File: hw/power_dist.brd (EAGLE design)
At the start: 80 x 50 mm, 72 parts, among them J1 JST-ZH6SMT_VERT, J2 JST-PH4SMT_VERT, J3 JST-PH5VERT, P1 XT30P, P2 XT30P, P3 XT30P, P4 XT30P, P5 XT30P, P6 XT30P, P7 XT90PW-M, Q1 PSMN4R8-100BSEJ, Q2 PSMN4R8-100BSEJ, Q3 PSMN4R8-100BSEJ, Q4 MF-DSC-SOT233-BSS138, Q5 MF-DSC-SOT233-MMBT3906, Q6 MF-DSC-SOT233-MMBT3904, U1 MAX15062AATA+T, U2 STM32G474CEU6, U3 LM5066IPMHE/NOPB, U4 TCAN334G

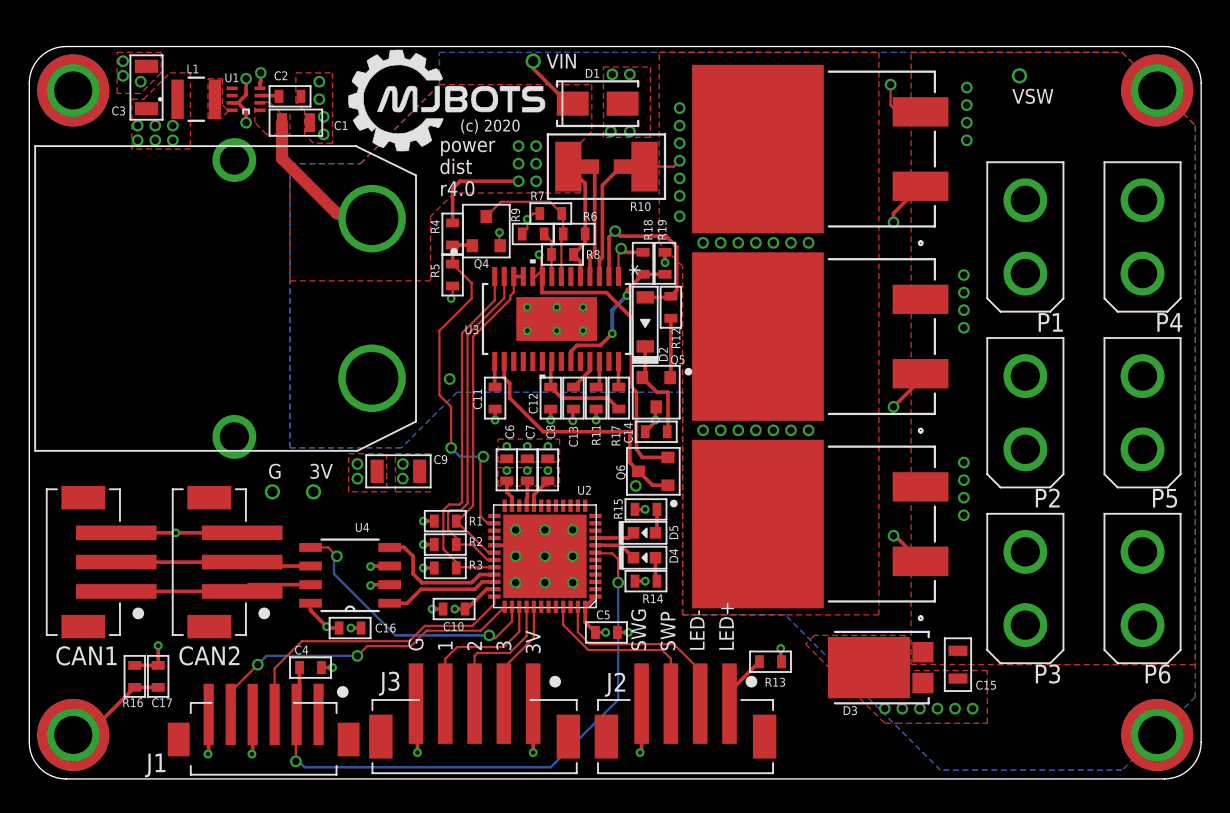
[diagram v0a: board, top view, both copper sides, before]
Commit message: Work towards functioning r4
* Beginnings of firmware
* Initial README and CHANGES
* Start on r4.1 w/ fixed D3 footprint
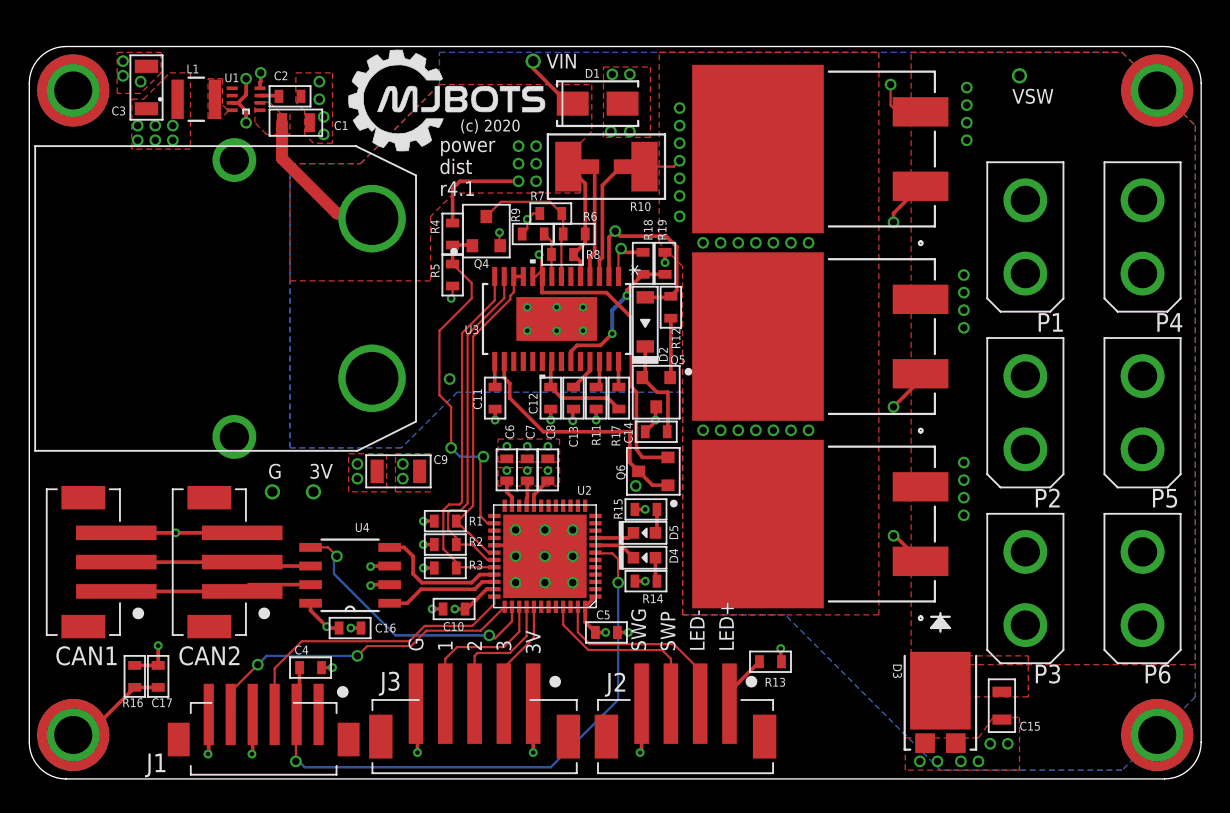
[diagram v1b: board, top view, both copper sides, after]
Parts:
- D3: value FSV10150V -> FSV10150VTO277-3L_ONS-L; device power_dist:TO277-3L_ONS -> power_dist:TO277-3L_ONS-L
- moved D3 4.66 mm to (62.2, 5.20), turned to 0 degrees
- moved C15 4.10 mm to (66.4, 5.00)
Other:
- board text added: "power dist r4.1"
- board text removed: "power dist r4.0"
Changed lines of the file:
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@@
 <text x="28" y="43.8" size="1" layer="21" font="vector" align="top-left">power
 dist
-r4.0</text>
+r4.1</text>
 <text x="29.4" y="45" size="0.8" layer="21" font="vector" ratio="10" align="top-left">(c) 2020</text>
 <polygon width="0.05" layer="25">
@@
 <attribute name="VENDOR" value="Vishay" x="38.8" y="46.1" size="1.778" layer="27" display="off"/>
 </element>
-<element name="D3" library="power_dist" package="TO277-3L_ONS" value="FSV10150V" x="58.2" y="7.6" smashed="yes" rot="R90">
-<attribute name="BUILT_BY" value="EMA_Jessica" x="58.2" y="7.6" size="1.778" layer="27" rot="R90" display="off"/>
-<attribute name="COPYRIGHT" value="Copyright (C) 2018 Accelerated Designs. All rights reserved" x="58.2" y="7.6" size="1.778" layer="27" rot="R90" display="off"/>
-<attribute name="MANUFACTURER_PART_NUMBER" value="FSV10150V" x="58.2" y="7.6" size="1.778" layer="27" rot="R90" display="off"/>
-<attribute name="MPN" value="FSV10150V" x="58.2" y="7.6" size="1.778" layer="27" rot="R90" display="off"/>
-<attribute name="NAME" x="55.5234" y="4.365" size="0.6" layer="25" ratio="10" rot="SR0"/>
-<attribute name="POPULATE" value="1" x="58.2" y="7.6" size="1.778" layer="27" rot="R90" display="off"/>
-<attribute name="SOURCELIBRARY" value="ON_Semiconductor_2019-12-30" x="58.2" y="7.6" size="1.778" layer="27" rot="R90" display="off"/>
-<attribute name="VENDOR" value="ON Semiconductor" x="58.2" y="7.6" size="1.778" layer="27" rot="R90" display="off"/>
+<element name="D3" library="power_dist" package="TO277-3L_ONS-L" value="FSV10150VTO277-3L_ONS-L" x="62.2" y="5.2" smashed="yes">
+<attribute name="BUILT_BY" value="EMA_Jessica" x="62.2" y="5.2" size="1.778" layer="27" display="off"/>
+<attribute name="COPYRIGHT" value="Copyright (C) 2018 Accelerated Designs. All rights reserved" x="62.2" y="5.2" size="1.778" layer="27" display="off"/>
+<attribute name="MANUFACTURER_PART_NUMBER" value="FSV10150V" x="62.2" y="5.2" size="1.778" layer="27" display="off"/>
+<attribute name="MPN" value="FSV10150V" x="62.2" y="5.2" size="1.778" layer="27" display="off"/>
+<attribute name="NAME" x="58.965" y="7.8766" size="0.6" layer="25" ratio="10" rot="SR270"/>
+<attribute name="POPULATE" value="1" x="62.2" y="5.2" size="1.778" layer="27" display="off"/>
+<attribute name="SOURCELIBRARY" value="ON_Semiconductor_2019-12-30" x="62.2" y="5.2" size="1.778" layer="27" display="off"/>
+<attribute name="VENDOR" value="ON Semiconductor" x="62.2" y="5.2" size="1.778" layer="27" display="off"/>
 </element>
 <element name="Q1" library="power_dist" package="D2PAK_SOT404_NEX" value="PSMN4R8-100BSEJ" x="54" y="30.2" smashed="yes" rot="R90">
@@
 <attribute name="POPULATE" value="1" x="39.4" y="41.8" size="1.778" layer="27" display="off"/>
 </element>
-<element name="C15" library="mfpassives" package="C0805" value="1uF 100V" x="63.4" y="7.8" smashed="yes" rot="R270">
-<attribute name="DIELECTRIC" value="" x="63.4" y="7.8" size="1.778" layer="27" rot="R270" display="off"/>
-<attribute name="HOUSEPART" value="" x="63.4" y="7.8" size="1.778" layer="27" rot="R270" display="off"/>
-<attribute name="MF" value="MURATA" x="63.4" y="7.8" size="1.778" layer="27" rot="R270" display="off"/>
-<attribute name="MPN" value="GCM21BC72A105KE36L" x="63.4" y="7.8" size="1.778" layer="27" rot="R270" display="off"/>
-<attribute name="NAME" x="64.6" y="6.1" size="0.6" layer="25" font="vector" ratio="10"/>
-<attribute name="POPULATE" value="1" x="63.4" y="7.8" size="1.778" layer="27" rot="R270" display="off"/>
-<attribute name="TOLERANCE" value="" x="63.4" y="7.8" size="1.778" layer="27" rot="R270" display="off"/>
-<attribute name="URL" value="" x="63.4" y="7.8" size="1.778" layer="27" rot="R270" display="off"/>
-<attribute name="VOLTAGE" value="" x="63.4" y="7.8" size="1.778" layer="27" rot="R270" display="off"/>
+<element name="C15" library="mfpassives" package="C0805" value="1uF 100V" x="66.4" y="5" smashed="yes" rot="R270">
+<attribute name="DIELECTRIC" value="" x="66.4" y="5" size="1.778" layer="27" rot="R270" display="off"/>
+<attribute name="HOUSEPART" value="" x="66.4" y="5" size="1.778" layer="27" rot="R270" display="off"/>
+<attribute name="MF" value="MURATA" x="66.4" y="5" size="1.778" layer="27" rot="R270" display="off"/>
+<attribute name="MPN" value="GCM21BC72A105KE36L" x="66.4" y="5" size="1.778" layer="27" rot="R270" display="off"/>
+<attribute name="NAME" x="67.6" y="3.3" size="0.6" layer="25" font="vector" ratio="10"/>
+<attribute name="POPULATE" value="1" x="66.4" y="5" size="1.778" layer="27" rot="R270" display="off"/>
+<attribute name="TOLERANCE" value="" x="66.4" y="5" size="1.778" layer="27" rot="R270" display="off"/>
+<attribute name="URL" value="" x="66.4" y="5" size="1.778" layer="27" rot="R270" display="off"/>
+<attribute name="VOLTAGE" value="" x="66.4" y="5" size="1.778" layer="27" rot="R270" display="off"/>
 </element>
 <element name="J3" library="power_dist" package="JST_B5B_PH-SM4-TB(LF)(SN)" value="JST-PH5VERT" x="30.4" y="2.6" smashed="yes" rot="R180">
@@
 <contactref element="C3" pad="P$2"/>
 <contactref element="D1" pad="2"/>
+<contactref element="D3" pad="1"/>
 <contactref element="D3" pad="2"/>
-<contactref element="D3" pad="1"/>
 <contactref element="R9" pad="P$2"/>
 <contactref element="R7" pad="P$2"/>
@@
 <vertex x="39.2" y="43.8"/>
 </polygon>
-<via x="58.4" y="4.8" extent="1-16" drill="0.5"/>
-<via x="59.6" y="4.8" extent="1-16" drill="0.5"/>
-<via x="60.8" y="4.8" extent="1-16" drill="0.5"/>
-<via x="62" y="4.8" extent="1-16" drill="0.5"/>
-<via x="63.2" y="4.8" extent="1-16" drill="0.5"/>
-<via x="64.4" y="4.8" extent="1-16" drill="0.5"/>
-<polygon width="0.1524" layer="1" thermals="no">
-<vertex x="53" y="9.2"/>
-<vertex x="58.4" y="3.8"/>
-<vertex x="59.2" y="3.8"/>
-<vertex x="65.4" y="3.8"/>
-<vertex x="65.4" y="7.4"/>
-<vertex x="59.8" y="7.4"/>
-<vertex x="59.8" y="9.8"/>
-<vertex x="53.6" y="9.8"/>
-</polygon>
+<via x="60.8" y="1.2" extent="1-16" drill="0.5"/>
+<via x="62" y="1.2" extent="1-16" drill="0.5"/>
+<via x="63.6" y="1.2" extent="1-16" drill="0.5"/>
+<via x="64.8" y="1.2" extent="1-16" drill="0.5"/>
+<via x="65.6" y="2.4" extent="1-16" drill="0.5"/>
+<via x="66.8" y="2.4" extent="1-16" drill="0.5"/>
 <contactref element="Q6" pad="P$2"/>
 <via x="34" y="32.2" extent="1-16" drill="0.3048"/>
@@
 <via x="43.4" y="35.25" extent="1-16" drill="0.3048"/>
 <wire x1="43.4" y1="35.95" x2="43.4" y2="35.25" width="0.254" layer="1"/>
+<polygon width="0.1524" layer="1" thermals="no">
+<vertex x="59.8" y="2.8"/>
+<vertex x="64.8" y="2.8"/>
+<vertex x="65.8" y="4.2"/>
+<vertex x="67.6" y="4.2"/>
+<vertex x="67.6" y="0.6"/>
+<vertex x="59.8" y="0.6"/>
+</polygon>
 </signal>
 <signal name="VCC" class="1">
@@
 <wire x1="41.9" y1="35.95" x2="40.65" y2="35.95" width="0.254" layer="1"/>
 <wire x1="40.65" y1="35.95" x2="40.4" y2="36.2" width="0.254" layer="1"/>
+<polygon width="0.1524" layer="1" thermals="no">
+<vertex x="61.4" y="8.4"/>
+<vertex x="68.2" y="8.4"/>
+<vertex x="68.2" y="5.6"/>
+<vertex x="61.4" y="5.6"/>
+</polygon>
 </signal>
 <signal name="VIN_SENSE">

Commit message: Draft r4.1 based on the LTC4380
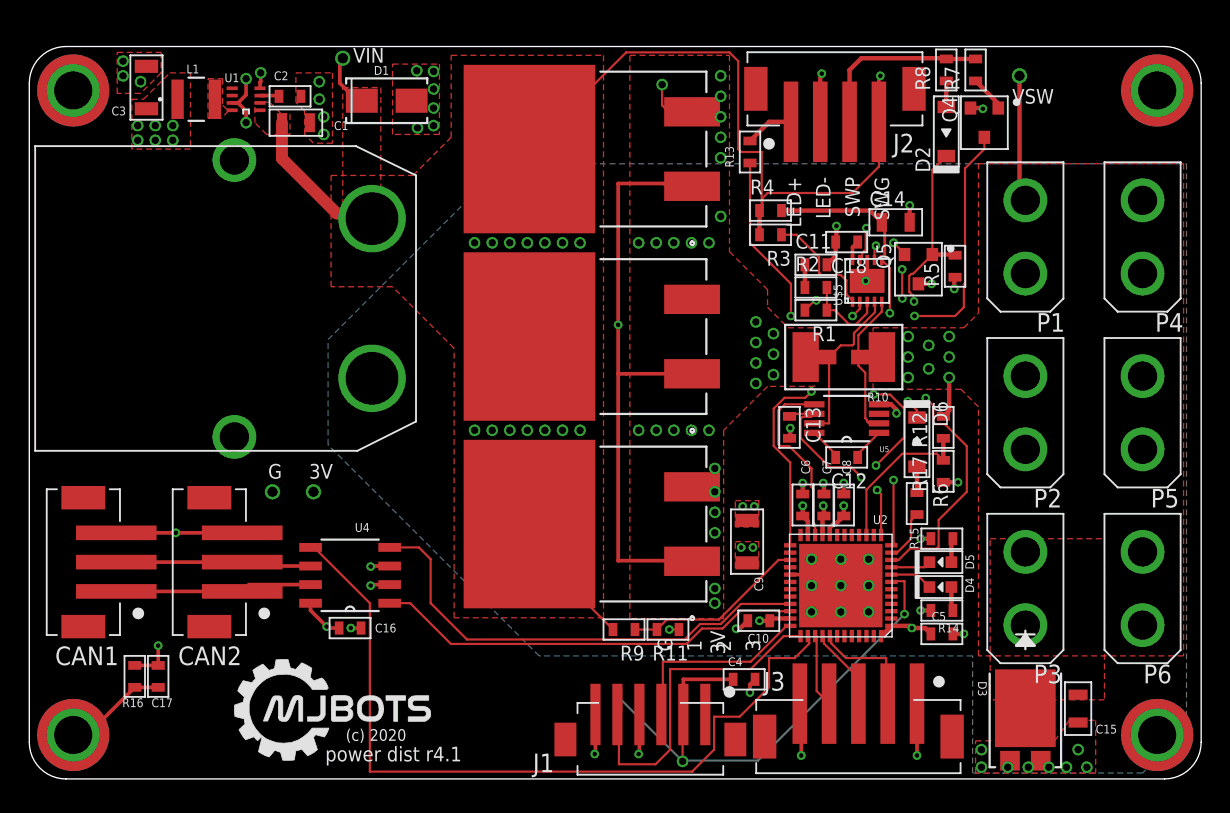
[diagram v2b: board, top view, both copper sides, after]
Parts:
- removed Q6: MF-DSC-SOT233-MMBT3904, mfdiscretesemi:SOT-23-3
- removed R18, R19: DNP, mfpassives:R0603
- removed U3: LM5066IPMHE/NOPB, power_dist:MXA28A_TEX
- added C18: 0.1uF, mfpassives:C0603
- added D6: MF-DIO-SOD123-1N4148, mfdiscretesemi:SOD-123
- added U$5: LTC4830, power_dist:DFN10
- added U5: LT1787HVIMS8PBF, LT1787HVIMS8PBF:MSOP-8_MS
- C11: value 1uF -> (none)
- C12: value 1uF -> DNP
- C13: value 0.01uF -> 0.1uF
- C14: value 0.01uF -> 1uF 100V; device mfpassives:C0603 -> mfpassives:C0805
- Q4: value MF-DSC-SOT233-BSS138 -> MF-DSC-SOT233-MMBT3904
- Q5: value MF-DSC-SOT233-MMBT3906 -> MMBT5401 100V
- R1, R2, R3: value 10k -> (none)
- R10: value 0.3mOhm -> 0.5mOhm
- R11: value 24k 1% -> 200k 1%
- R12: value 1k 1% -> 3M 1%
- R17: value DNP -> 200k 1%
- R4: value 140k 1% -> 10k
- R5: value 40.2k 1% -> 200k
- R6: value 100k 1% -> 1k
- R7: value 40.2k 1% -> 2M
- R8: value 140k 1% -> 500k
- R9: value 6.49k 1% -> 3M 1%
- moved J2 45.9 mm to (55.0, 47.4), turned to 0 degrees
- moved R13 34.8 mm to (49.2, 42.8), turned to 270 degrees
- moved Q4 34.8 mm to (65.2, 44.8), turned to 270 degrees
- moved R5 34.3 mm to (63.2, 35.0), turned to 90 degrees
- moved R3 31.8 mm to (50.6, 37.1)
- moved R2 30.8 mm to (53.7, 33.5), turned to 0 degrees
- moved R7 30.6 mm to (64.6, 48.4), turned to 90 degrees
- moved R6 29.8 mm to (60.6, 18.8), turned to 270 degrees
- moved C4 29.6 mm to (48.8, 6.80)
- moved R1 29.1 mm to (53.7, 32.0)
- moved R8 29.1 mm to (62.6, 48.4), turned to 90 degrees
- moved R9 27.7 mm to (40.6, 10.2)
- moved J1 26.4 mm to (42.4, 2.40)
- moved J3 26.2 mm to (56.6, 2.60)
- moved D2 24.3 mm to (62.6, 44.2)
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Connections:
- removed net N$16: Q5.P$1, R12.P$2
- removed net N$3: Q6.P$1, Q6.P$3, U3.16
- removed net PSHDN: Q4.P$1, R4.P$2, R5.P$1, U2.26
- removed net SCL: R2.P$1, U2.31, U3.13
- removed net SDA: R1.P$1, U2.30, U3.11, U3.12
- removed net SMBA: R3.P$1, U2.32, U3.14
- removed net VDD: C12.P$1, R17.P$1, U3.21
- removed net VIN_SENSE: R8.P$2, R9.P$1, U3.8
- new net FLT: U$5.7, U2.13
- new net GATE: Q1.1, Q2.1, Q3.1, R1.P$2
- new net ISAMP: U2.22, U5.5
- new net ISAMP_BIAS: C13.P$1, U2.12, U5.6
- new net LTC_EN: Q5.P$2, U$5.9
- new net LTC_VCC: C14.P$1, R4.P$2, U$5.2, U$5.6
- new net N$17: D2.ANODE, R8.P$1
- new net N$18: D6.ANODE, R6.P$1
- new net PGND: C15.P$2, D3.1, D3.2, P1.1, P2.1, P3.1, P4.1, P5.1, P6.1, P7.1
- new net PWR_OVERRIDE: R6.P$2, U2.11
- new net SNS_PWR_SW: Q4.P$3, U2.10
- new net VIN_SAMP: R11.P$2, R9.P$1, U2.27
- new net VSWITCHED_SAMP: R12.P$1, R17.P$2, U2.15
- net +24V: now also J2.4, Q1.2, Q2.2, Q3.2, R3.P$2, R9.P$2; no longer R10.1, R6.P$1, R8.P$1, U3.5
- net GND: now also C18.P$2, J2.2, R11.P$1, R17.P$1, R5.P$1, U$5.8, U$5.P$1, U5.4; no longer C12.P$2, C15.P$2, D3.1, D3.2, J2.4, P1.1, P2.1, P3.1, P4.1, P5.1, P6.1, P7.1, Q6.P$2, R11.P$2, R19.P$2, R5.P$2, R7.P$2, R9.P$2, U3.10, U3.9
- net N$10: now also R3.P$1, U$5.1; no longer R11.P$1, U3.26
- net N$11: now also Q4.P$1, R7.P$1; no longer C13.P$1, U3.25
- net N$12: now also C18.P$1, U$5.10; no longer R17.P$2, U3.28
- net N$13: now also D6.CATHODE, Q5.P$1, R5.P$2; no longer C14.P$1, Q5.P$2
- net N$5: now also R1.P$1, R2.P$2, U$5.3; no longer D2.ANODE, Q1.1, Q2.1, Q3.1, R12.P$1, U3.2
- net N$6: now also C12.P$1, U5.1; no longer R18.P$2, R19.P$1, U3.23
- net N$7: now also C12.P$2, U5.8; no longer C11.P$1, U3.15
- net N$9: now also C11.P$1, R2.P$1; no longer Q4.P$3, R6.P$2, R7.P$1, U3.7
- net PWR_LED: now also R13.P$2, U2.25; no longer J2.2, U2.47
- net PWR_SW: now also R7.P$2, R8.P$2; no longer U2.45
- net VCC: no longer R1.P$2, R13.P$2, R2.P$2, R3.P$2
- net VIN_POST: now also Q1.3, Q2.3, Q3.3, R10.1; no longer Q1.2, Q2.2, Q3.2, R10.2
- net VSENSE_HIGH: now also U$5.4, U5.7; no longer U3.4
- net VSENSE_LOW: now also U$5.5, U5.2; no longer U3.3
- net VSWITCHED: now also R10.2, R12.P$2; no longer Q1.3, Q2.3, Q3.3, R18.P$1, U3.1
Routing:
- net N$5: track 84.0 -> 5.82 mm, vias 4 -> 0
- net GATE: track 0.00 -> 56.3 mm, vias 0 -> 2
- net SNS_PWR_SW: track 0.00 -> 40.3 mm, vias 0 -> 2
- net +24V: track 30.1 -> 70.3 mm, vias 6 -> 15
- net CAN_SHDN: track 18.8 -> 54.1 mm, vias 2 -> 0
- net VSWITCHED: track 37.5 -> 11.5 mm, vias 14 -> 8
- net FLT: track 0.00 -> 25.3 mm, vias 0 -> 6
- net PSHDN: track 24.9 -> 0.00 mm, vias 2 -> 0
- net SMBA: track 24.8 -> 0.00 mm
- net CAN_RX: track 9.08 -> 32.7 mm
- net SCL: track 23.6 -> 0.00 mm
- net SDA: track 22.5 -> 0.00 mm
- net CAN_TX: track 7.76 -> 29.5 mm
- net PWR_LED: track 13.4 -> 31.5 mm, vias 0 -> 2
- net LTC_VCC: track 0.00 -> 17.7 mm, vias 0 -> 2
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- added copper zone on layer 2, net +24V
- added copper zone on layer 1, net PGND
- added copper zone on layer 15, net PGND
- added copper zone on layer 16, net PGND
- added copper zone on layer 2, net VIN_POST
- added copper zone on layer 2, net VSWITCHED
- removed copper zone on layer 15, net +24V
- removed copper zone on layer 16, net GND
- removed copper zone on layer 15, net VIN_POST
- removed copper zone on layer 15, net VSWITCHED
